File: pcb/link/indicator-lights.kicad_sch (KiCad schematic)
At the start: 28 parts, among them IC1 IS31FL3236A-TQLS4-TR, J4 68021-204HLF

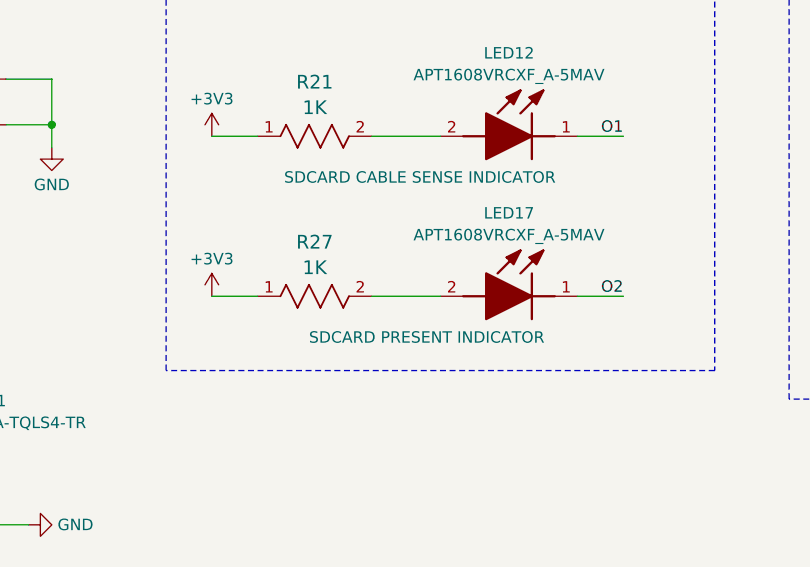
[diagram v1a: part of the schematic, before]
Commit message: rename/move around SDCard LEDs (closes #109)
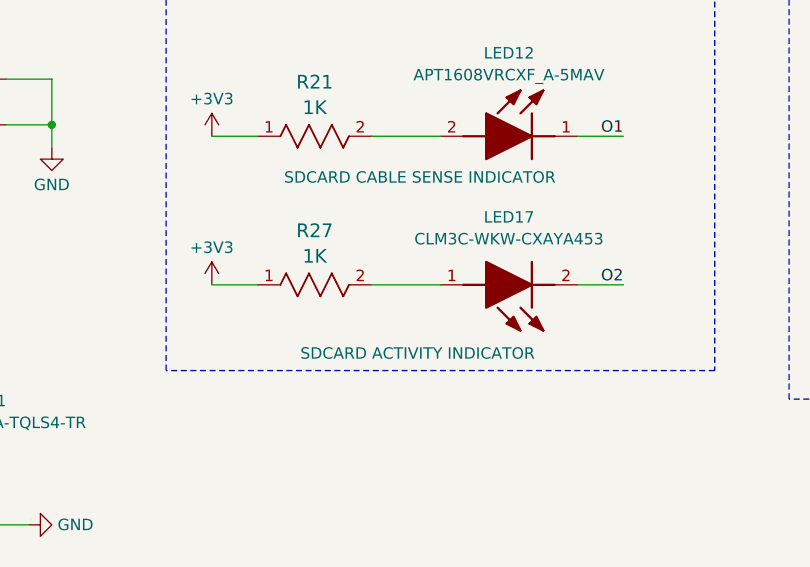
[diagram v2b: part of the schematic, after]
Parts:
- removed LED17: APT1608VRCXF_A-5MAV, OroLink:APT1608VRCXFA5MAV, symbol OroLink:APT1608VRCXF_A-5MAV
- added LED17: CLM3C-WKW-CXAYA453, OroLink:CLM3CWKWCXAYA453, symbol OroLink:CLM3C-WKW-CXAYA453
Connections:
- net O2: now also LED17.2 (K)
- net at R27.2: now also LED17.1 (A)
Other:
- moved on the sheet: R27
